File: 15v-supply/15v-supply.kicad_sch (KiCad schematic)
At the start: 23 parts, among them J1 Screw_Terminal_01x03

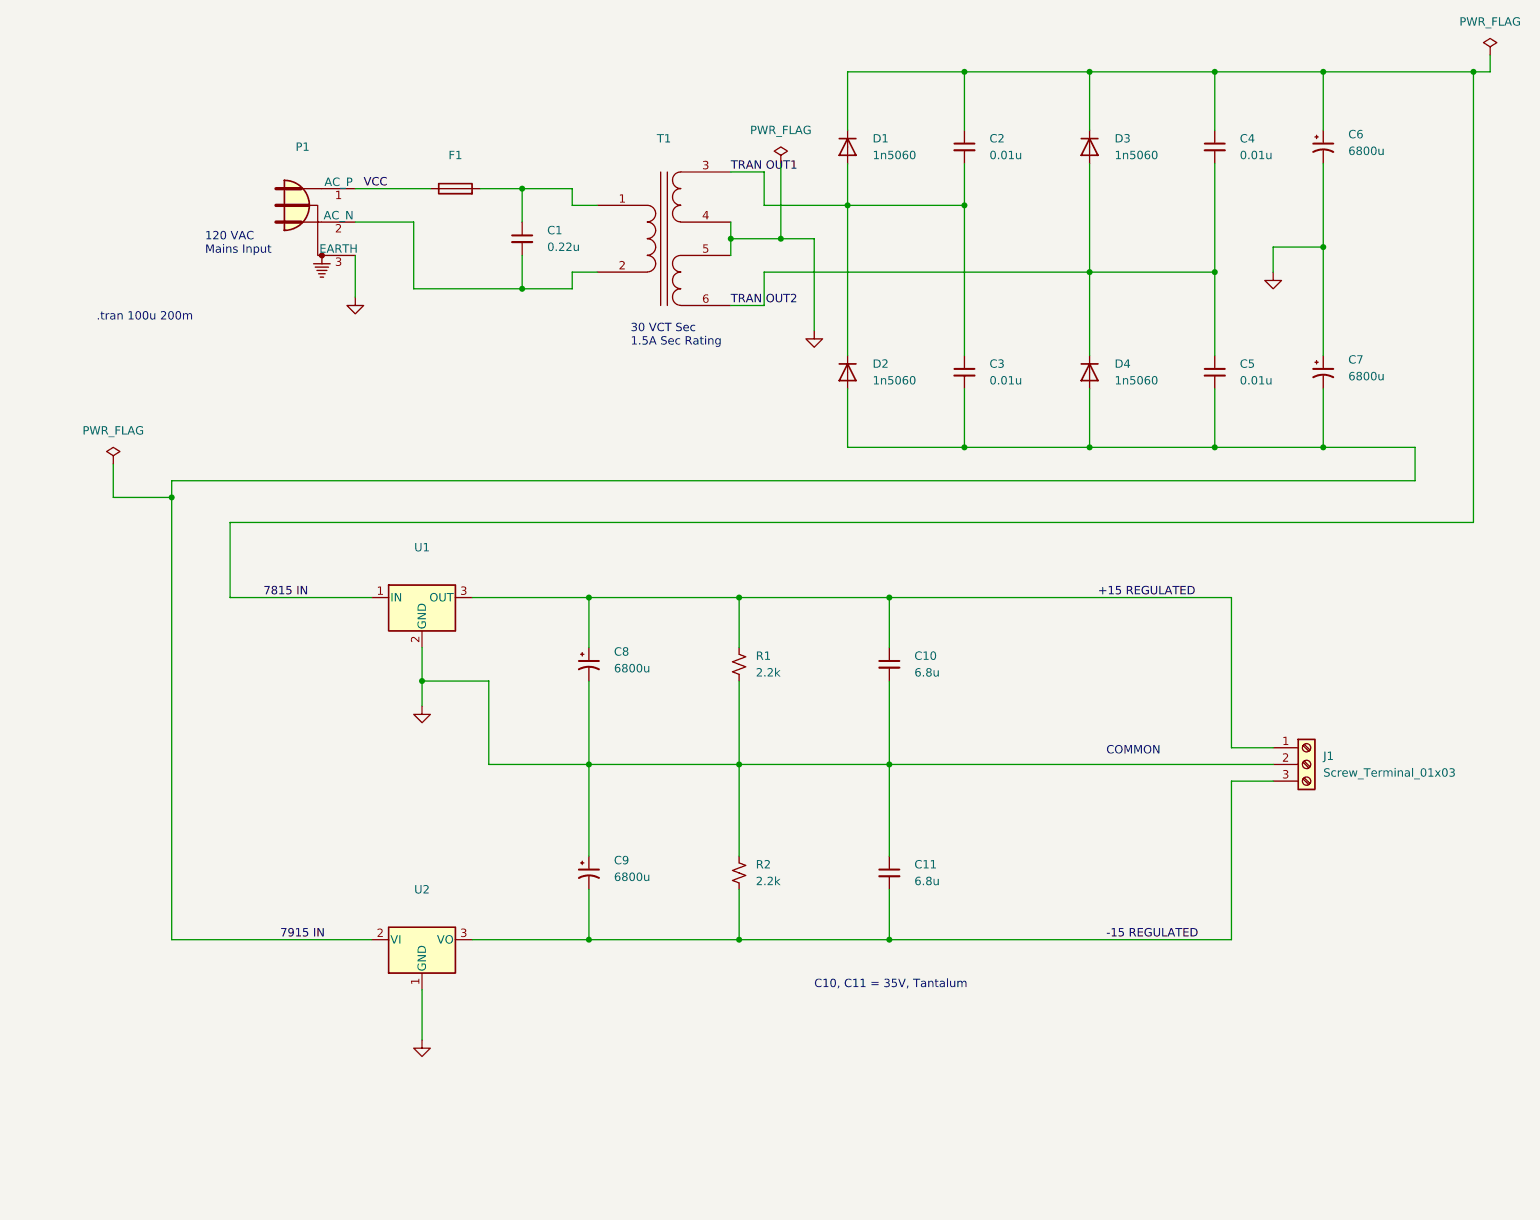
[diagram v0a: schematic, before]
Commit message: Changes to 15v supply including symbol annotation, BOM, footprints, and folder reorg
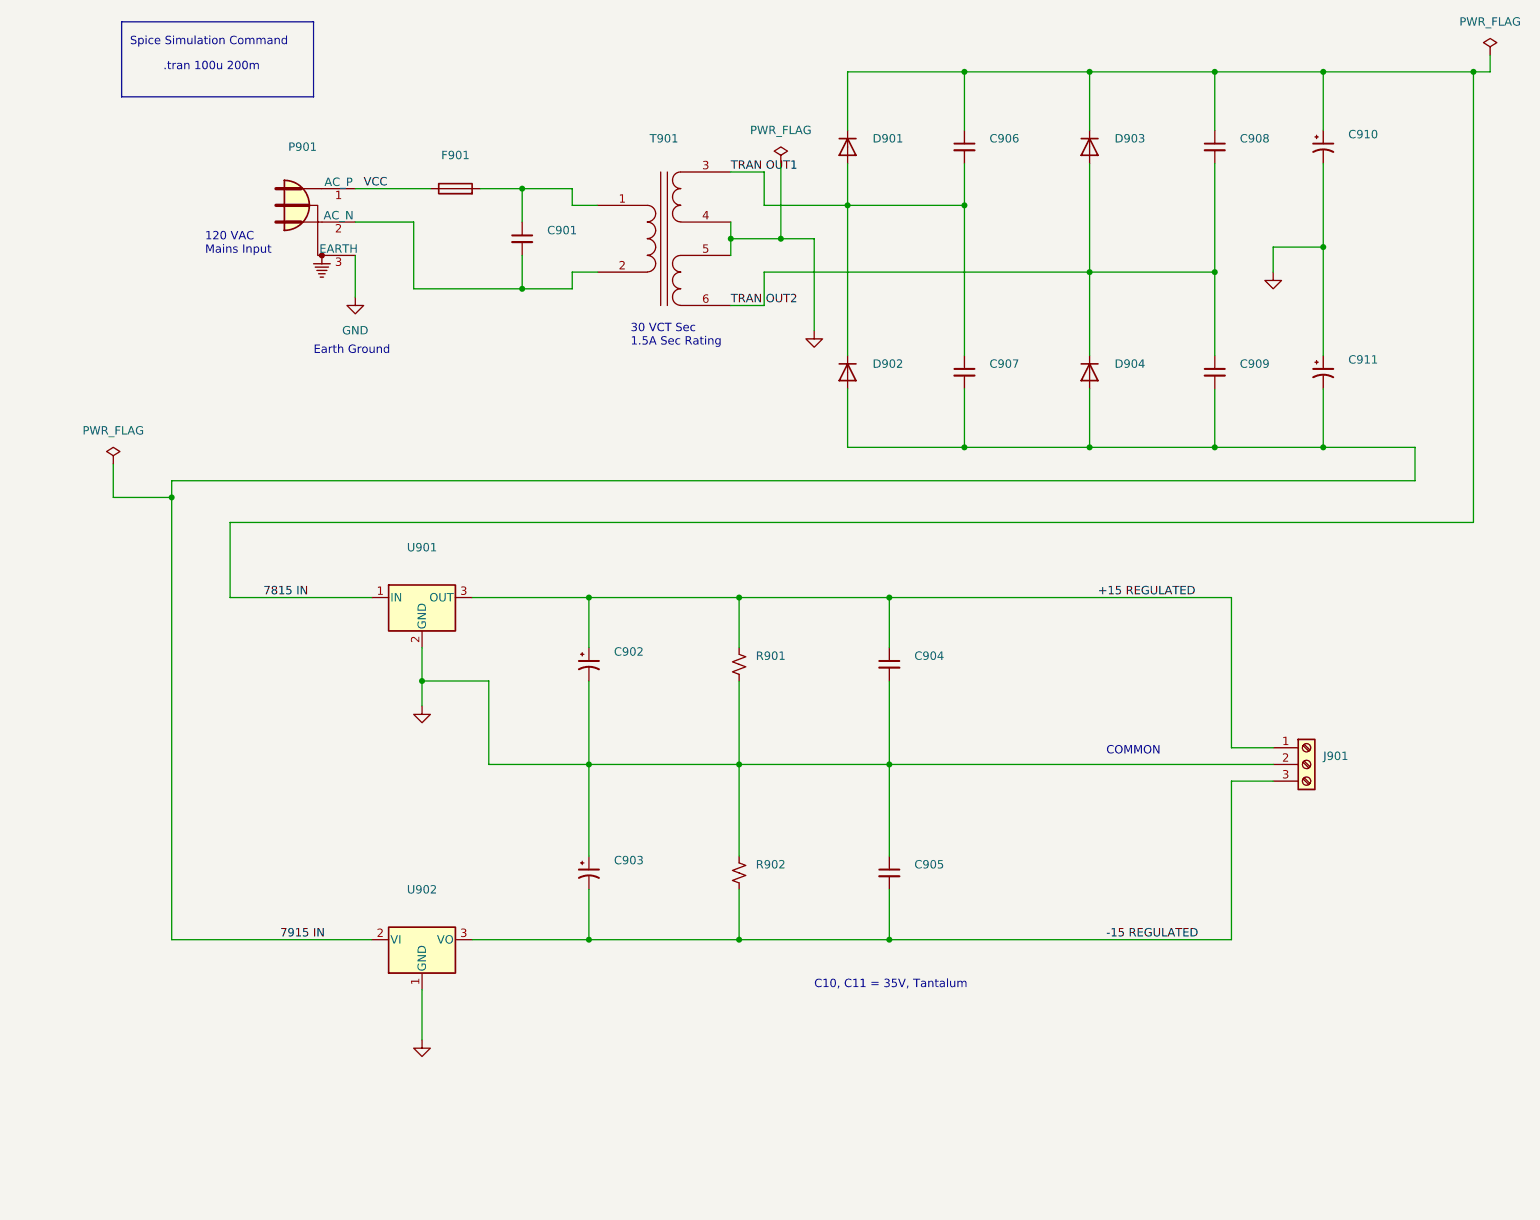
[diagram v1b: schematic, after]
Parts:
- C901: renamed from C1; value 0.22u -> (none); footprint Capacitor_THT:C_Axial_L5.1mm_D3.1mm_P7.50mm_Horizontal -> (none)
- C902: renamed from C8; value 6800u -> (none)
- C903: renamed from C9; value 6800u -> (none)
- C904: renamed from C10; value 6.8u -> (none)
- C905: renamed from C11; value 6.8u -> (none)
- C906: renamed from C2; value 0.01u -> (none)
- C907: renamed from C3; value 0.01u -> (none)
- C908: renamed from C4; value 0.01u -> (none)
- C909: renamed from C5; value 0.01u -> (none)
- C910: renamed from C6; value 6800u -> (none)
- C911: renamed from C7; value 6800u -> (none)
- D901: renamed from D1; value 1n5060 -> (none); footprint DO15-12 -> (none); Spice_Lib_File 1n5060.lib -> 15v-supply-spice\1n5060.lib
- D902: renamed from D2; value 1n5060 -> (none); footprint DO15-12 -> (none); Spice_Lib_File 1n5060.lib -> 15v-supply-spice\1n5060.lib
- D903: renamed from D3; value 1n5060 -> (none); footprint DO15-12 -> (none); Spice_Lib_File 1n5060.lib -> 15v-supply-spice\1n5060.lib
- D904: renamed from D4; value 1n5060 -> (none); footprint DO15-12 -> (none); Spice_Lib_File 1n5060.lib -> 15v-supply-spice\1n5060.lib
- J901: renamed from J1; value Screw_Terminal_01x03 -> (none); footprint TerminalBlock_4Ucon:TerminalBlock_4Ucon_1x03_P3.50mm_Horizontal -> (none)
- P901: renamed from P1; now left out of the parts list
- R901: renamed from R1; value 2.2k -> (none)
- R902: renamed from R2; value 2.2k -> (none)
- T901: renamed from T1; Spice_Lib_File xformer.lib -> 15v-supply-spice\xformer.lib
- U901: renamed from U1; Spice_Lib_File regulators.lib -> 15v-supply-spice\regulators.lib
- U902: renamed from U2; Spice_Lib_File regulators.lib -> 15v-supply-spice\regulators.lib
- renumbered F1 to F901
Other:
- note added: "Earth Ground"
- note added: "Spice Simulation Command"

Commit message: more improvements to 15v-supply
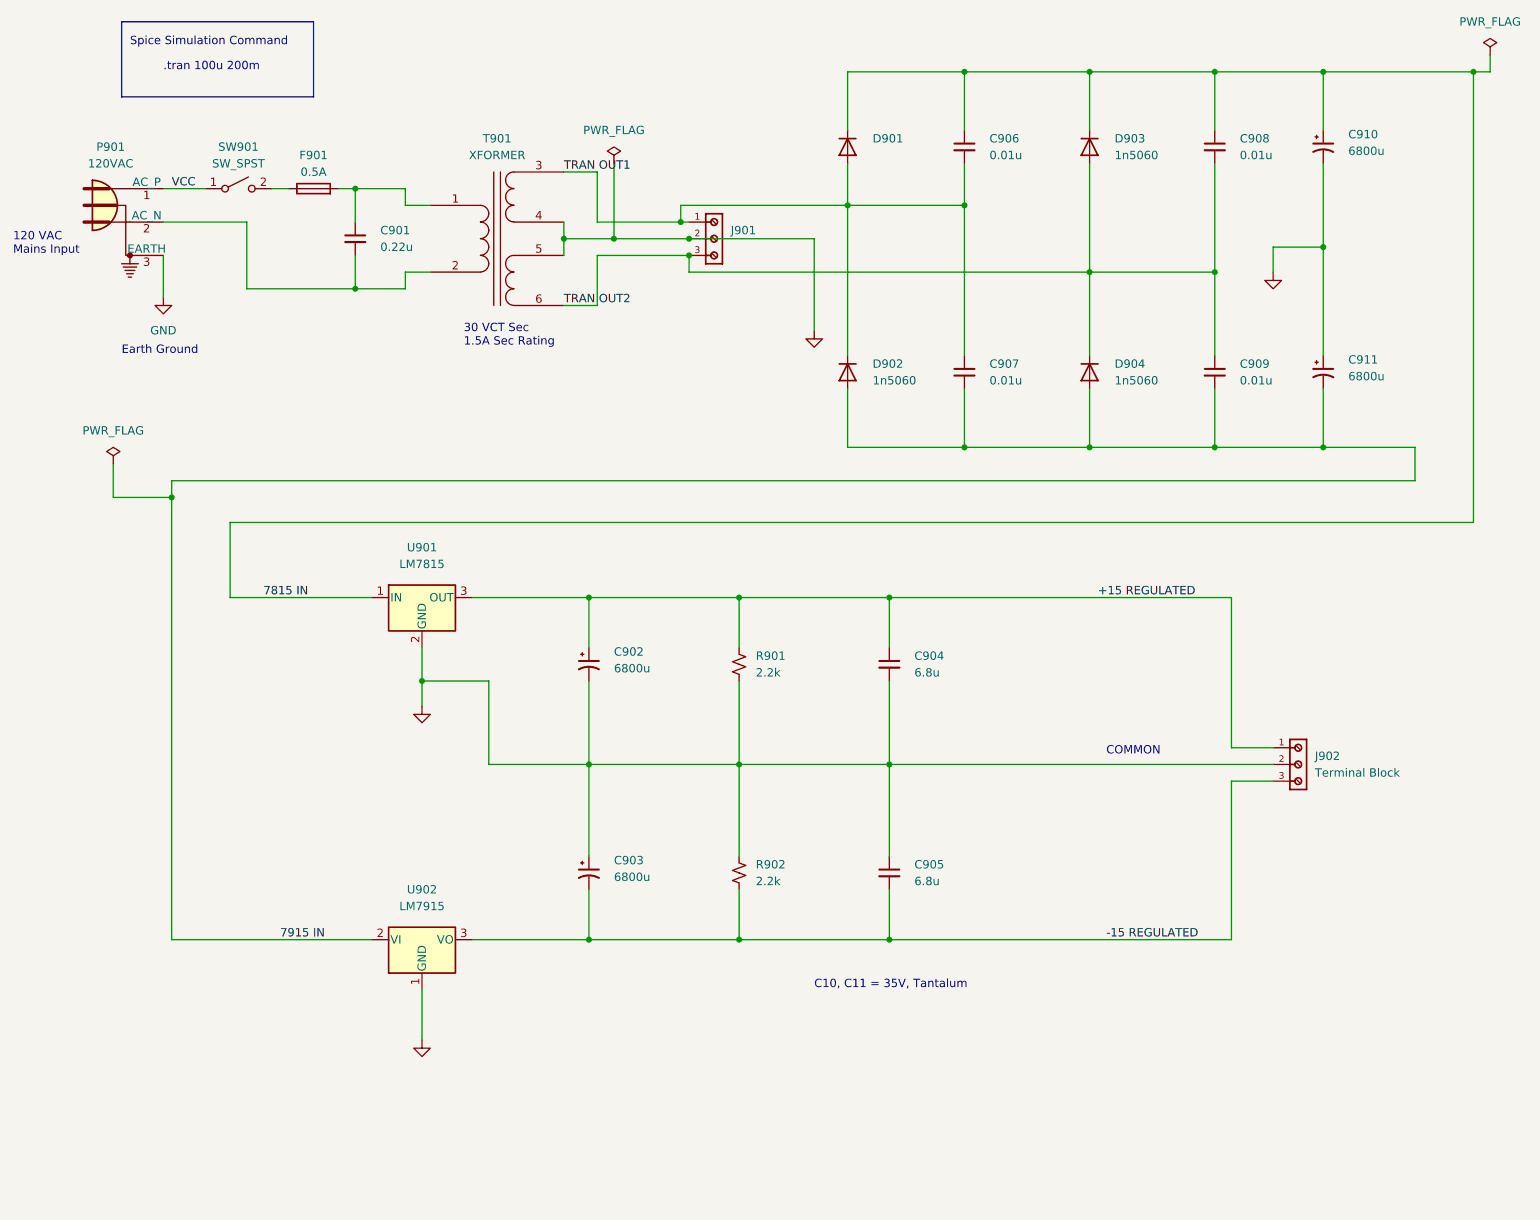
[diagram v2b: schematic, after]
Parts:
- removed J901: (no value), symbol Connector:Screw_Terminal_01x03
- added J901: (no value), symbol 691103110003:691103110003
- added J902: Terminal Block, 691103110003, symbol 691103110003:691103110003
- added SW901: SW_SPST, symbol Switch:SW_SPST
- C901: value (none) -> 0.22u; footprint (none) -> Capacitor_THT:C_Rect_L4.6mm_W5.5mm_P2.50mm_MKS02_FKP02
- C902, C903, C910, C911: value (none) -> 6800u; footprint (none) -> 6800u Footprint:UVR1H682MRD6
- C904, C905: value (none) -> 6.8u; footprint (none) -> Capacitor_THT:CP_Radial_D5.0mm_P2.50mm
- C906, C907, C908, C909: value (none) -> 0.01u; footprint (none) -> Capacitor_THT:C_Radial_D8.0mm_H7.0mm_P3.50mm
- D902, D903, D904: value (none) -> 1n5060; footprint (none) -> Diode_THT:D_DO-34_SOD68_P7.62mm_Horizontal
- F901: value (none) -> 0.5A
- P901: value (none) -> 120VAC
- R901, R902: value (none) -> 2.2k; footprint (none) -> Resistor_THT:R_Axial_DIN0207_L6.3mm_D2.5mm_P7.62mm_Horizontal
- T901: value (none) -> XFORMER
- U901: value (none) -> LM7815; footprint (none) -> Package_TO_SOT_THT:TO-220-3_Horizontal_TabUp
- U902: value (none) -> LM7915; footprint (none) -> Package_TO_SOT_THT:TO-220-3_Horizontal_TabUp
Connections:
- net +15 REGULATED: now also J902.1
- net -15 REGULATED: now also J902.3
- net GND: now also J901.2, J902.2
- net TRAN OUT1: now also J901.1
- net TRAN OUT2: now also J901.3
- net VCC: now also SW901.1 (A); no longer F901.1
- new net: F901.1, SW901.2 (B)
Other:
- moved on the sheet: C901, F901, P901, T901

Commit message: 15v-supply routed and poured
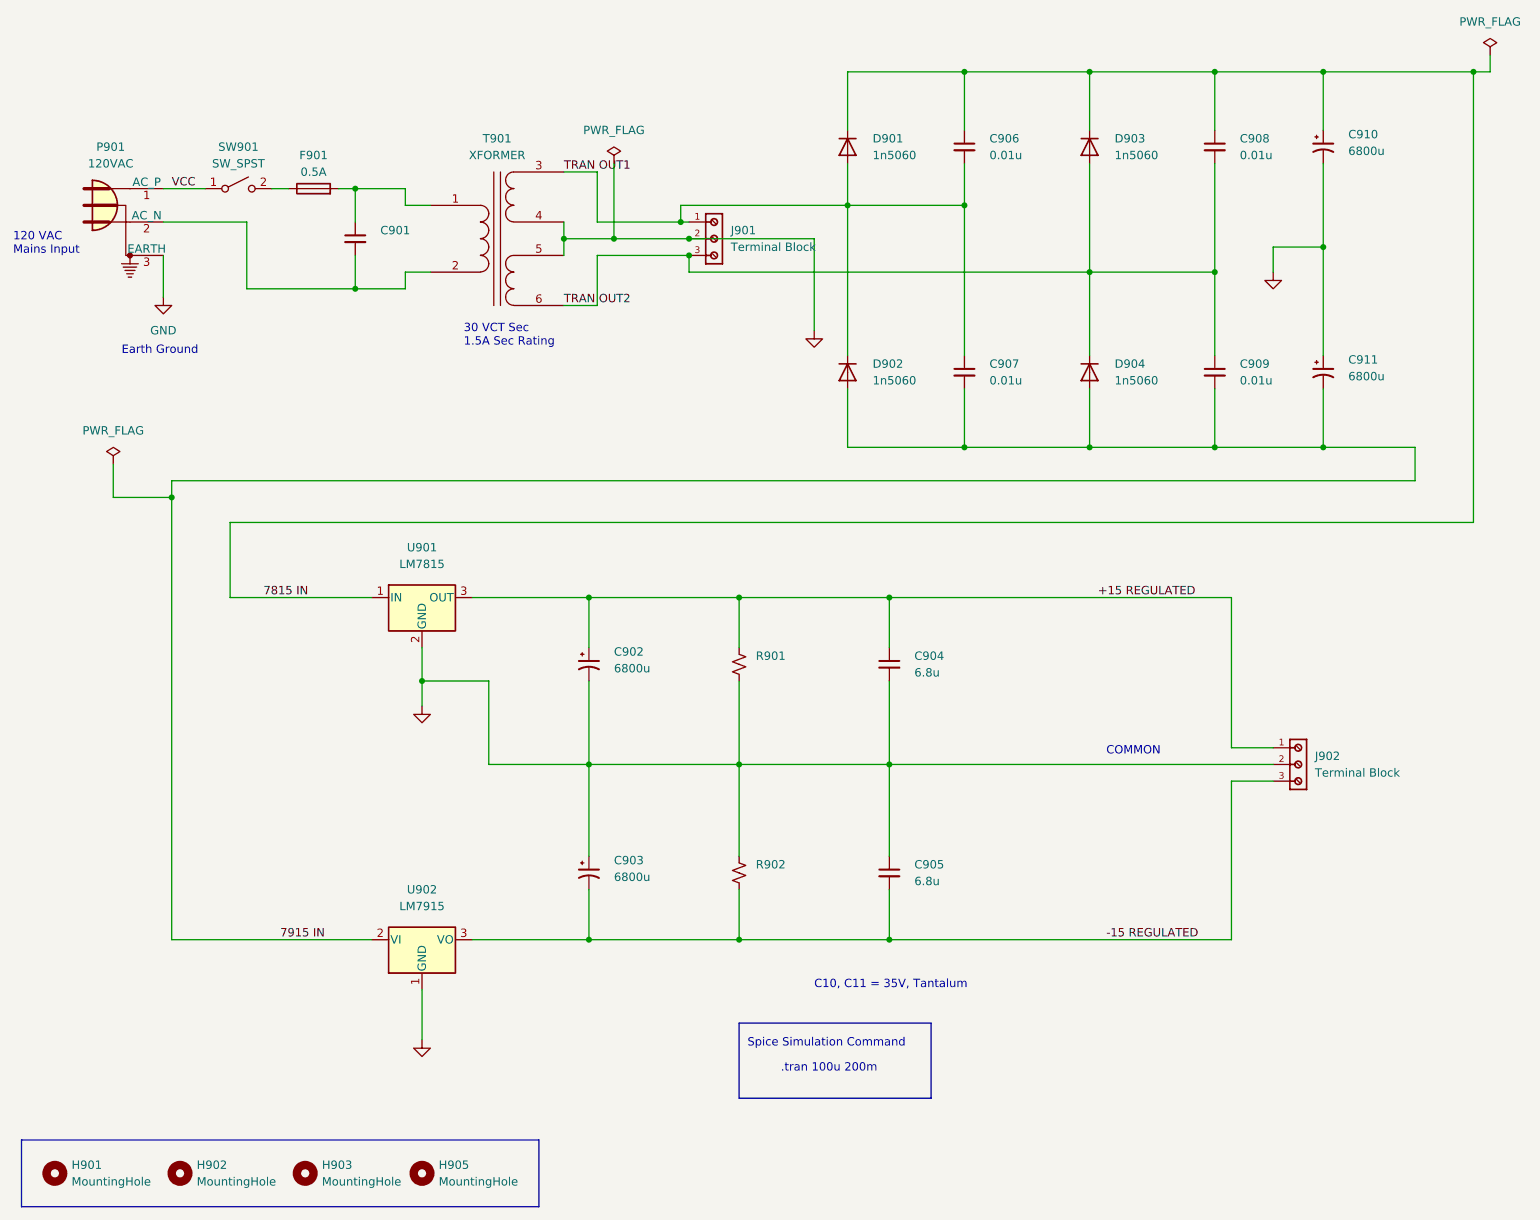
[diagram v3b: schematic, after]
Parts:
- added H901, H902, H903, H905: MountingHole, MountingHole:MountingHole_3.2mm_M3, symbol Mechanical:MountingHole
- C901: value 0.22u -> (none); footprint Capacitor_THT:C_Rect_L4.6mm_W5.5mm_P2.50mm_MKS02_FKP02 -> (none)
- C902, C903, C910, C911: footprint 6800u Footprint:UVR1H682MRD6 -> 15v-supply:6800u-UVR1H682MRD6
- C906, C907, C908, C909: footprint Capacitor_THT:C_Radial_D8.0mm_H7.0mm_P3.50mm -> 15v-supply:C_Rect_L6.0mm_W3.5mm_P3.5mm_QYX1H103JTP3TA
- D901: value (none) -> 1n5060; footprint (none) -> Diode_THT:D_DO-41_SOD81_P7.62mm_Horizontal; Spice_Node_Sequence 2 1 -> (none)
- D902, D903, D904: footprint Diode_THT:D_DO-34_SOD68_P7.62mm_Horizontal -> Diode_THT:D_DO-41_SOD81_P7.62mm_Horizontal; Spice_Node_Sequence 2 1 -> (none)
- J901: value (none) -> Terminal Block; footprint (none) -> 15v-supply:terminal-block-691103110003; symbol 691103110003:691103110003 -> terminal-block:691103110003
- J902: footprint 691103110003 -> 15v-supply:terminal-block-691103110003; symbol 691103110003:691103110003 -> terminal-block:691103110003
- R901, R902: value 2.2k -> (none); footprint Resistor_THT:R_Axial_DIN0207_L6.3mm_D2.5mm_P7.62mm_Horizontal -> (none)
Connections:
- net 7815 IN: now also D901.2 (Anode), D903.2 (Anode); no longer D901.C, D903.C
- net 7915 IN: now also D902.1 (Cathode), D904.1 (Cathode); no longer D902.A, D904.A
- net TRAN OUT1: now also D901.1 (Cathode), D902.2 (Anode); no longer D901.A, D902.C
- net TRAN OUT2: now also D903.1 (Cathode), D904.2 (Anode); no longer D903.A, D904.C
